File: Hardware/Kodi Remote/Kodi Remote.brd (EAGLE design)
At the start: 55 x 41.9 mm, 24 parts

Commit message: Update Kodi Remote
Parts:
- added IR_SEND: (no value), adafruit:LED3MM
- added R3: 200, SparkFun-Resistors:0805
- IR_SIGNAL: value (none) -> IR_RECV; device adafruit:CHIPLED_0805 -> adafruit:LED3MM
- R1, R2: value (none) -> 200
- RF_SIGNAL: value (none) -> RF; device adafruit:CHIPLED_0805 -> adafruit:LED3MM
- moved RF_SIGNAL 32.8 mm to (17.7, 51.7), turned to 270 degrees
- moved R2 27.8 mm to (17.8, 47.6), turned to 180 degrees
- moved IR_SIGNAL 10.0 mm to (17.9, 25.8), turned to 270 degrees
- moved R1 0.63 mm to (22.9, 22.9), turned to 180 degrees
- moved TSOP1838 0.57 mm to (17.9, 32.0), turned to 90 degrees
- turned IR1 to 45 degrees
- turned IR3 to 315 degrees
- turned IR5 to 315 degrees
- turned IR8 to 45 degrees
- renumbered LED4 to IR4, ULN1 to ULN2803
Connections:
- new net N$4: IR_SEND.A, R3.1
- net 0: no longer ULN2803.1, ULN2803.2, ULN2803.3, ULN2803.4, ULN2803.5, ULN2803.6, ULN2803.7, ULN2803.8
- net 15: now also R3.2, ULN2803.1, ULN2803.2, ULN2803.3, ULN2803.4, ULN2803.5, ULN2803.6, ULN2803.7, ULN2803.8; no longer JP4.3
- net 16: now also JP4.3
- net GND: now also IR_SEND.K
- net N$1: now also RF_SIGNAL.K; no longer RF_SIGNAL.C
- net N$3: now also IR_SIGNAL.K; no longer IR_SIGNAL.C
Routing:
- net 15: track 11.9 -> 65.8 mm
- net 16: track 3.07 -> 55.4 mm
- net 0: track 40.6 -> 3.19 mm, vias 1 -> 0
- net 14: track 51.7 -> 30.3 mm
- net N$4: track 0.00 -> 8.19 mm, vias 0 -> 1
- net GND: track 107.9 -> 114.0 mm
- net 2: track 27.2 -> 22.1 mm
- net VCC: track 128.7 -> 125.6 mm, vias 0 -> 1
- net N$3: track 2.49 -> 4.74 mm
- net N$12: track 10.1 -> 11.2 mm
- net N$14: track 19.6 -> 20.5 mm
- net N$9: track 12.3 -> 13.1 mm
- net N$1: track 2.49 -> 3.12 mm
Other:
- board text added: "12"
- board text added: "13"
- board text added: "14"
- board text added: "16"
- board text added: "2"
- board text added: "4"
- board text added: "5"
- board text added: "G"
- board text added: "Kodi Remote"
- board text added: "NC"
- board text added: "T1838"
- board text added: "VCC"
- board text added: "Vin"

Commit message: Update Kodi Remote to use locked version of Sandy Esp
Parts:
- U$2: value MINI-ESP -> MINI-ESPMINI-ESP-LOCK; device My Eagle Lib:MINI-ESP -> My Eagle Lib:MINI-ESP-LOCK

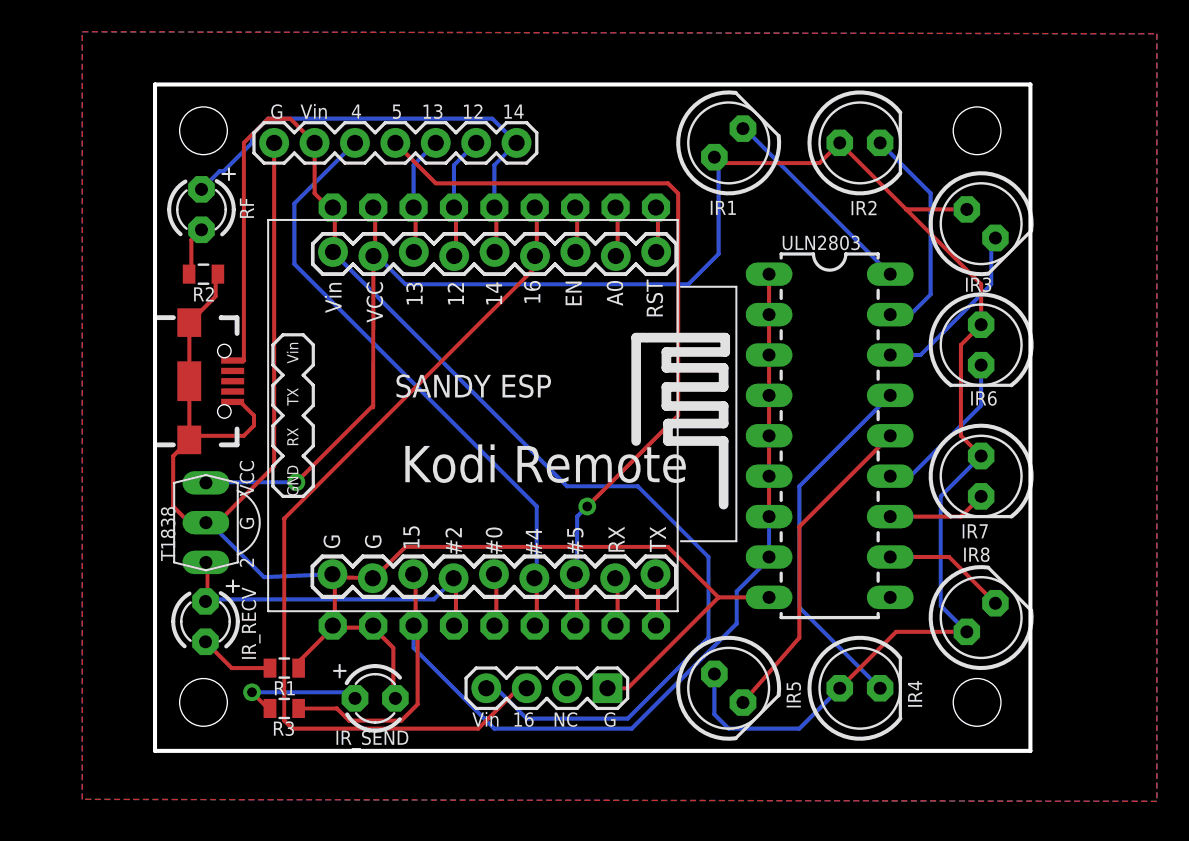
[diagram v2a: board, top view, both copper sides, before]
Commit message: Update Kodi after first prototype
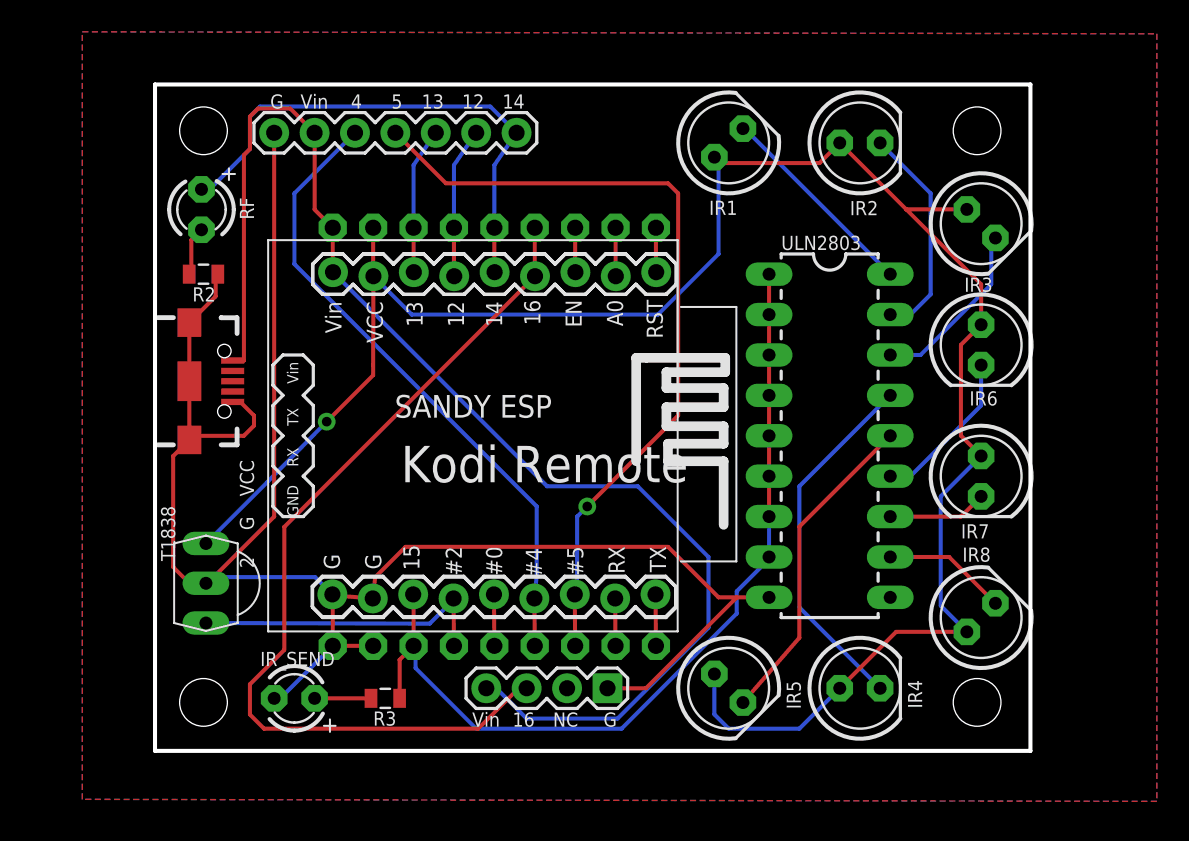
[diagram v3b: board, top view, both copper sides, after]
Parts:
- removed IR_SIGNAL: IR_RECV, adafruit:LED3MM
- removed R1: 200, SparkFun-Resistors:0805
- moved R3 6.38 mm to (29.2, 21.0)
- moved IR_SEND 5.08 mm to (23.5, 21.0), turned to 180 degrees
- moved TSOP1838 3.81 mm to (17.9, 28.2)
- moved JP1 1.27 mm to (36.1, 50.5)
- moved JP3 1.27 mm to (36.1, 24.3)
- moved U$2 1.27 mm to (34.5, 37.5)
- moved JP2 0.63 mm to (22.2, 56.5)
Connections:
- removed net N$3: IR_SIGNAL.K, R1.2
- net 2: no longer IR_SIGNAL.A
- net GND: no longer R1.1
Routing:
- net 15: track 66.0 -> 55.3 mm
- net GND: track 114.1 -> 119.7 mm
- net N$3: track 4.74 -> 0.00 mm
- net N$4: track 8.19 -> 3.54 mm, vias 1 -> 0
- net 2: track 22.1 -> 19.3 mm
- net 14: track 30.3 -> 33.1 mm
- net 12: track 7.75 -> 9.47 mm
- net 4: track 38.5 -> 40.2 mm
- net VIN: track 81.3 -> 83.0 mm
- net 16: track 55.3 -> 56.9 mm
- net 13: track 7.75 -> 9.21 mm
- net 5: track 49.4 -> 50.4 mm
